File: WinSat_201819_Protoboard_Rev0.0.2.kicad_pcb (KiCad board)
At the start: 4 copper layers, 64 parts, among them J1 Conn_01x02_Female, J2 Conn_01x02_Female, J3 Conn_01x02_Female, J4 Conn_01x02_Female, J5 Conn_01x03_Female, J6 Conn_01x02_Female, P1 TPS82150, U1 SSM3K329R, U10 XBEE_PRO900, U2 SSM3K329R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

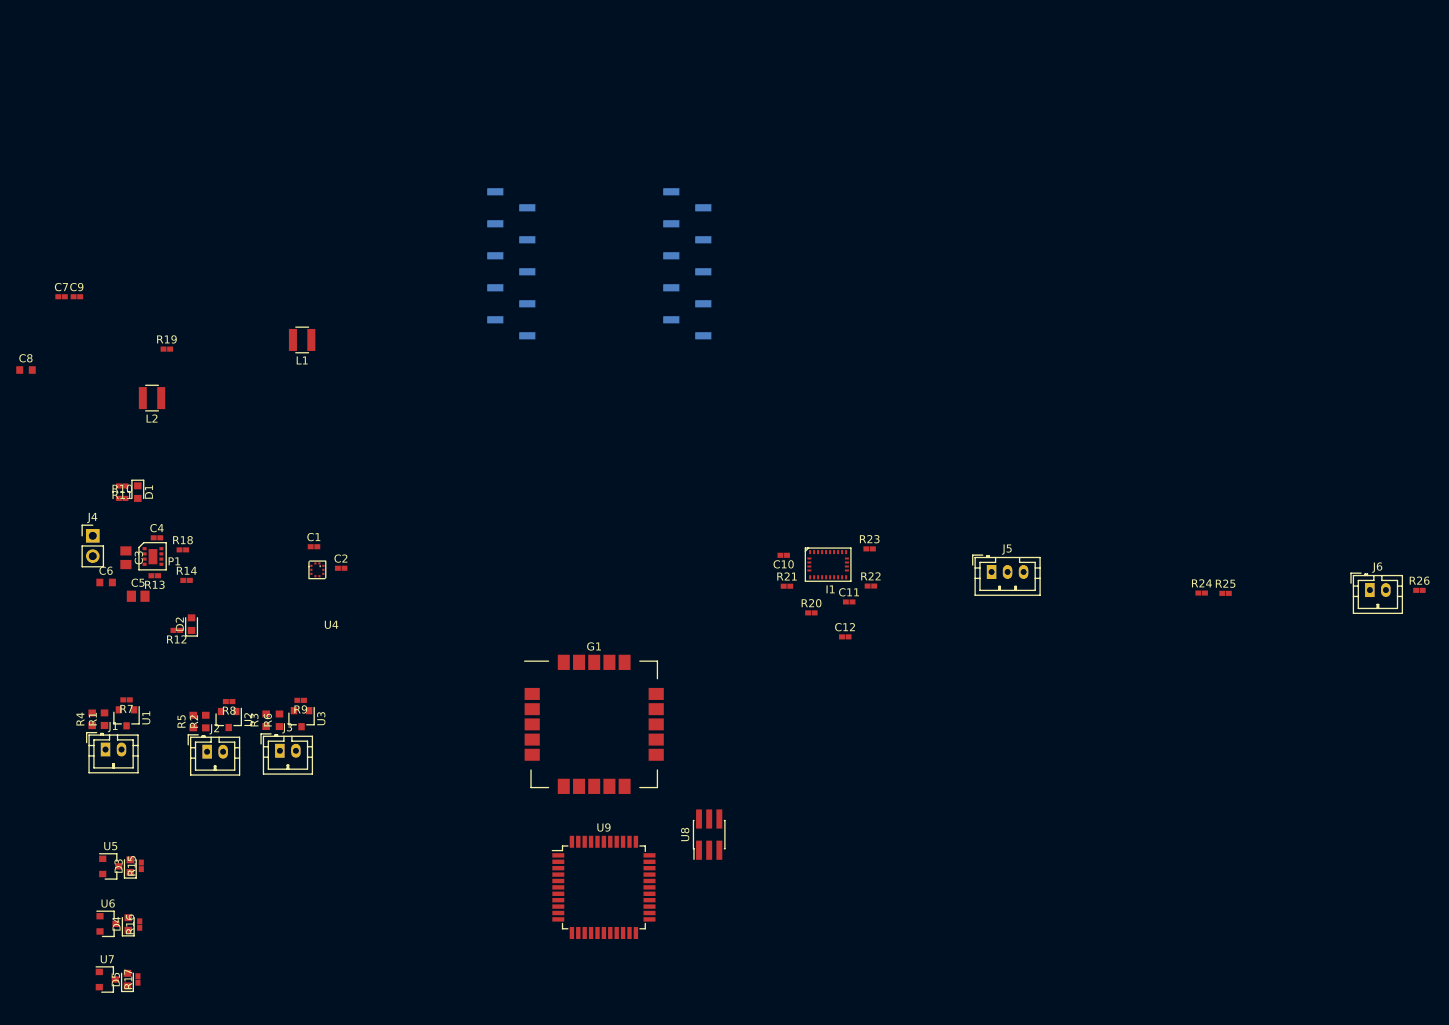
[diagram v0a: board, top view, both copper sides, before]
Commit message: net to power and pcb updates
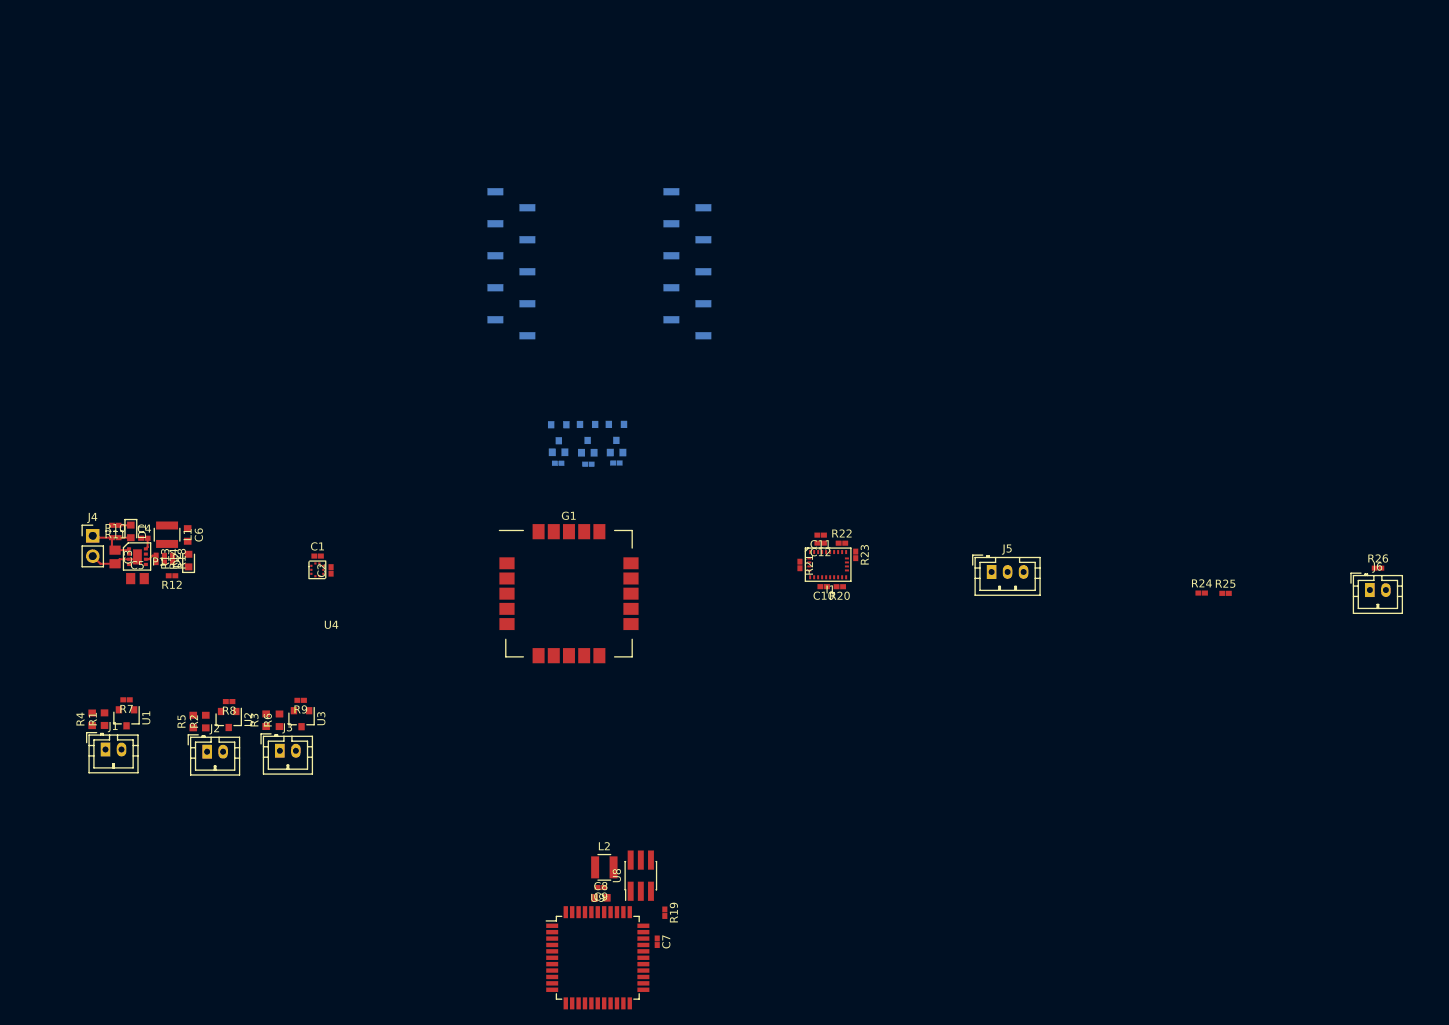
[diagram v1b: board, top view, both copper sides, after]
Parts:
- D3, D4, D5, R15, R16, R17, U5, U6, U7: moved to B.Cu
- moved C7 109.7 mm to (88.9, 181.7), turned to 270 degrees
- moved C9 98.7 mm to (81.9, 174.9), turned to 180 degrees
- moved C8 97.6 mm to (81.9, 176.2)
- moved R19 94.0 mm to (89.9, 178.0), turned to 270 degrees
- moved U7 93.4 mm to (83.8, 118.0), turned to 270 degrees
- moved D5 89.9 mm to (83.8, 120.5), turned to 180 degrees
- moved R17 88.0 mm to (83.8, 121.8), turned to 180 degrees
- moved U6 85.8 mm to (80.2, 118.0), turned to 270 degrees
- moved D4 82.3 mm to (80.2, 120.5), turned to 180 degrees
- moved L2 81.5 mm to (82.3, 172.4), turned to 180 degrees
- moved R16 80.4 mm to (80.3, 122.0), turned to 180 degrees
- moved U5 77.9 mm to (76.6, 118.0), turned to 270 degrees
- moved D3 74.4 mm to (76.6, 120.5), turned to 180 degrees
- moved R15 72.4 mm to (76.5, 121.9), turned to 180 degrees
- moved L1 29.6 mm to (27.6, 130.8), turned to 90 degrees
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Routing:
- net BAT_POS: track 0.00 -> 6.68 mm
- net GND: track 0.00 -> 6.58 mm
- net Net-(D1-Pad1): track 0.00 -> 1.55 mm
- net Net-(D1-Pad2): track 0.00 -> 1.54 mm
- net Net-(P1-Pad6): track 0.00 -> 1.47 mm
- net Net-(C4-Pad2): track 0.00 -> 1.42 mm

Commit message: Near Complete Prototype
Still needed:
Camera Control
Servo Control
Ground Plane
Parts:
- removed D3, D4, D5: LED, LED_SMD:LED_0603_1608Metric
- removed R15, R16, R17: 400 OHM, Resistor_SMD:R_0402_1005Metric
- removed U1, U2, U3, U5, U6, U7: SSM3K329R, Package_TO_SOT_SMD:SOT-23
- removed U8: JTAG-6PIN, Connector_PinHeader_1.27mm:PinHeader_2x03_P1.27mm_Vertical_SMD
- added J7: JTAG-6PIN, Connector_PinHeader_1.27mm:PinHeader_2x03_P1.27mm_Vertical_SMD, B.Cu at (77.0, 81.4)
- added Q1: SSM3K329R, Package_TO_SOT_SMD:SOT-23, F.Cu at (92.0, 116.8)
- added Q2: SSM3K329R, Package_TO_SOT_SMD:SOT-23, F.Cu at (84.8, 116.8)
- added Q3: SSM3K329R, Package_TO_SOT_SMD:SOT-23, F.Cu at (77.6, 116.8)
- C7, C8, C9, L2, R19, R24, R25, U9: moved to B.Cu
- moved R26 102.0 mm to (94.1, 78.5)
- moved J6 99.0 mm to (95.0, 83.8), turned to 90 degrees
- moved C7 92.3 mm to (74.9, 90.4)
- moved R19 92.2 mm to (75.7, 86.9)
- moved R25 92.2 mm to (84.5, 85.1)
- moved U9 91.3 mm to (82.3, 92.4), turned to 180 degrees
- moved L2 91.3 mm to (81.5, 81.1), turned to 0 degrees
- moved C9 91.3 mm to (82.0, 83.6), turned to 0 degrees
- moved C8 91.3 mm to (81.9, 84.9), turned to 180 degrees
- moved R24 88.1 mm to (86.6, 85.1)
- moved J1 87.0 mm to (94.6, 112.9), turned to 180 degrees
- moved R4 86.4 mm to (96.2, 116.7), turned to 270 degrees
- moved R1 83.6 mm to (94.7, 116.7), turned to 270 degrees
- moved R7 76.5 mm to (91.9, 119.1), turned to 0 degrees
- moved J2 70.8 mm to (87.4, 112.9), turned to 180 degrees
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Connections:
- net 3.3V renamed +3V3
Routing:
- net GND: track 6.58 -> 88.1 mm, vias 0 -> 23
- net +3V3: track 0.00 -> 58.6 mm, vias 0 -> 17
- net BAT_POS: track 6.68 -> 51.3 mm
- net MOSFET1_GPIO: track 0.00 -> 28.5 mm, vias 0 -> 1
- net MOSFET2_GPIO: track 0.00 -> 26.0 mm, vias 0 -> 1
- net IMU_SDA: track 0.00 -> 25.6 mm, vias 0 -> 2
- net MOSFET0_GPIO: track 0.00 -> 23.8 mm, vias 0 -> 1
- net GPS_TX-MCU_RX: track 0.00 -> 23.4 mm, vias 0 -> 1
- net GPS_RX-MCU_TX: track 0.00 -> 22.5 mm, vias 0 -> 1
- net IMU_SCL: track 0.00 -> 22.5 mm, vias 0 -> 2
- net XBEE_TX-MCU_RX: track 0.00 -> 14.6 mm
- net Net-(C5-Pad1): track 0.00 -> 13.6 mm
- net TEMP_SENSE-ADC: track 0.00 -> 13.3 mm
- net Net-(J7-Pad5): track 0.00 -> 7.72 mm
- net TACH_ADC: track 0.00 -> 7.16 mm
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- added copper zone on In1.Cu, net +3V3
- added copper zone on F.Cu, net BAT_POS
- added copper zone on In2.Cu, net GND
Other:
- board outline added: 36 x 62 mm
- net class Default: clearance 0.2 -> 0.0508; trace_width 0.25 -> 0.1
- rule trace_clearance: 0.2 -> 0.0508
- rule trace_min: 0.2 -> 0.006

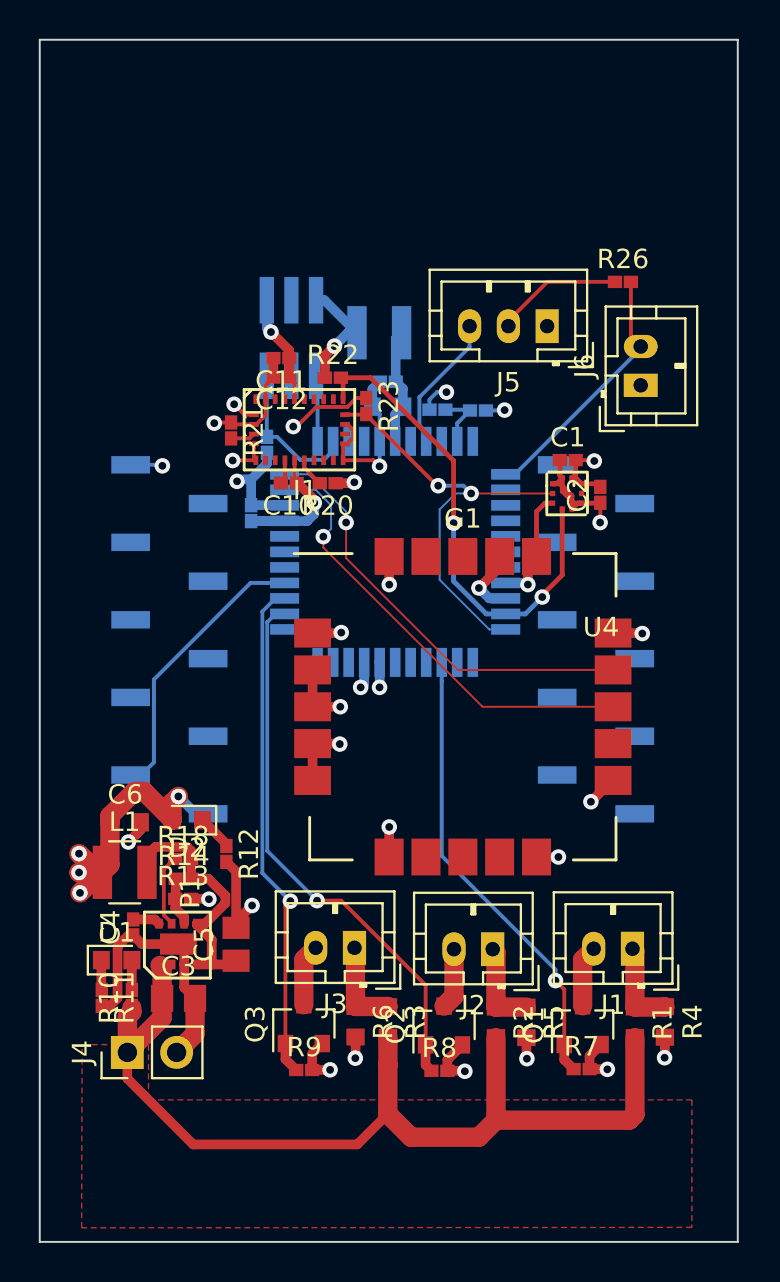
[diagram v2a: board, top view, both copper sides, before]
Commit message: V1.0.0
First Complete Revision

To Do:
-Double check schematic and PCB
-Increase width of some data lines
-Add ESD Protection
--Resistor and Diodes
--ESD Dissipation 1MOhm
-Trade study M2 vs M3* (*current)
-Check application notes for BNO055 to ensure that we are in spec (stresses, RF, and such.
-Misc.
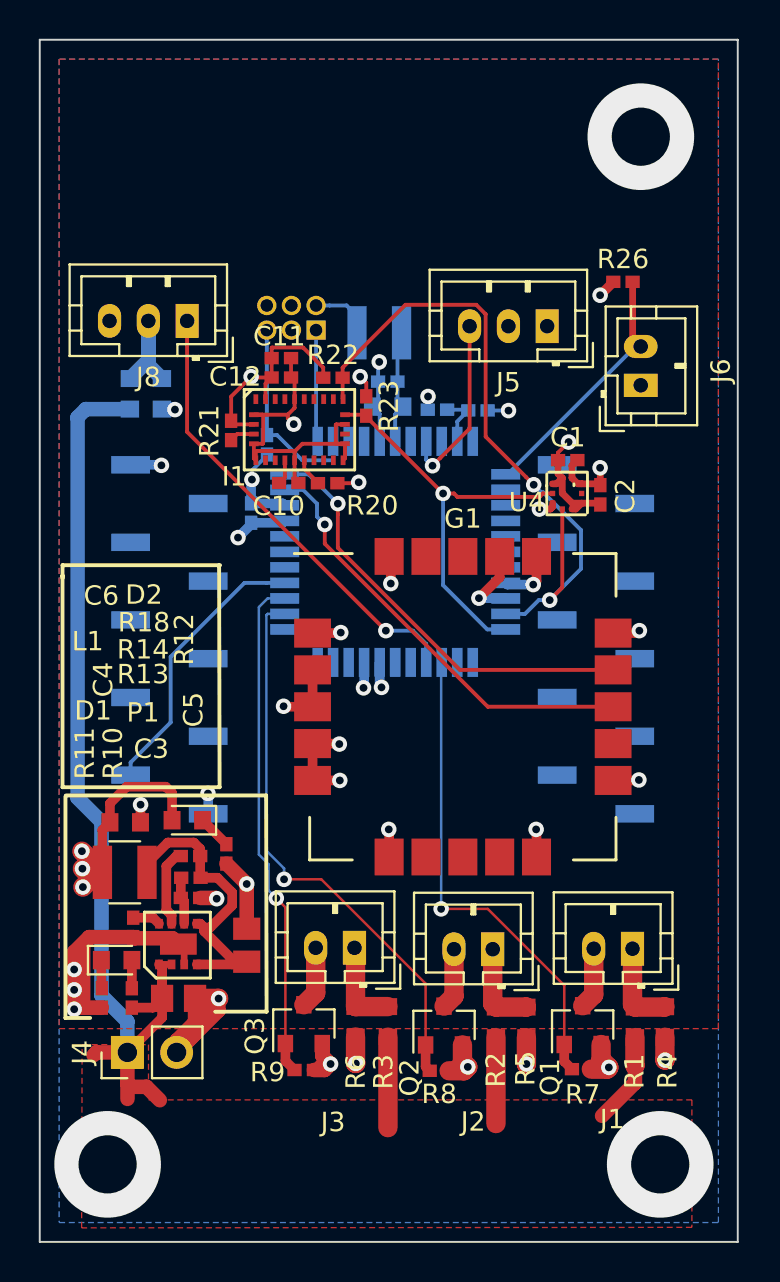
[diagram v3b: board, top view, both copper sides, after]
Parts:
- added J8: Conn_01x03_Female, Connector_JST:JST_PH_B3B-PH-K_1x03_P2.00mm_Vertical, F.Cu at (71.6, 80.5)
- added R15: R_Small, Resistor_SMD:R_0603_1608Metric, B.Cu at (68.7, 84.3)
- added R16: R_Small, Resistor_SMD:R_0603_1608Metric, B.Cu at (70.3, 84.3)
- C1, C10, C11, C12, C2, C4, C7, C9: footprint Capacitor_SMD:C_0402_1005Metric -> OSD335x-KiCad-master:Not_Broken_0402
- J7: footprint Connector_PinHeader_1.27mm:PinHeader_2x03_P1.27mm_Vertical_SMD -> Connector_PinHeader_1.27mm:PinHeader_2x03_P1.27mm_Horizontal
- R10, R11, R12, R13, R14, R18, R19, R20, R21, R22, R23, R24, R25, R26, R7, R8, R9: footprint Resistor_SMD:R_0402_1005Metric -> OSD335x-KiCad-master:Not_Broken_0402
- moved J7 1.33 mm to (78.2, 81.0)
- moved C5 0.55 mm to (74.7, 112.7)
- moved R18 0.40 mm to (71.8, 108.1)
- moved R13 0.38 mm to (71.8, 110.3)
- moved R14 0.38 mm to (71.8, 109.2)
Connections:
- U9 pad 15: Net-(U9-Pad15) -> SERVO_TCL
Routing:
- net SERVO_TCL: track 0.00 -> 23.5 mm, vias 0 -> 1
- net BAT_POS: track 51.3 -> 65.8 mm
- net IMU_SDA: track 25.6 -> 35.6 mm
- net GND: track 88.1 -> 97.9 mm, vias 23 -> 31
- net Net-(J8-Pad2): track 0.00 -> 6.63 mm
- net Net-(J7-Pad5): track 7.72 -> 10.3 mm
- net +3V3: track 58.6 -> 56.2 mm
- net Net-(J7-Pad1): track 3.41 -> 5.77 mm
- net TACH_ADC: track 7.16 -> 9.39 mm, vias 0 -> 1
- net MOSFET0_GPIO: track 23.8 -> 25.2 mm
- net Net-(C5-Pad1): track 13.6 -> 14.8 mm
- net IMU_SCL: track 22.5 -> 21.5 mm, vias 2 -> 1
- net GPS_TX-MCU_RX: track 23.4 -> 22.5 mm
- net MOSFET1_GPIO: track 28.5 -> 29.1 mm
- added copper zone on B.Cu, net GND
- added copper zone on F.Cu, net GND
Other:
- net class Default: clearance 0.0508 -> 0.127; trace_width 0.1 -> 0.2
- rule trace_clearance: 0.0508 -> 0.127
- rule trace_min: 0.006 -> 0.127
- rule via_min_drill: 0.3 -> 0.254
- rule via_min_size: 0.4 -> 0.4572

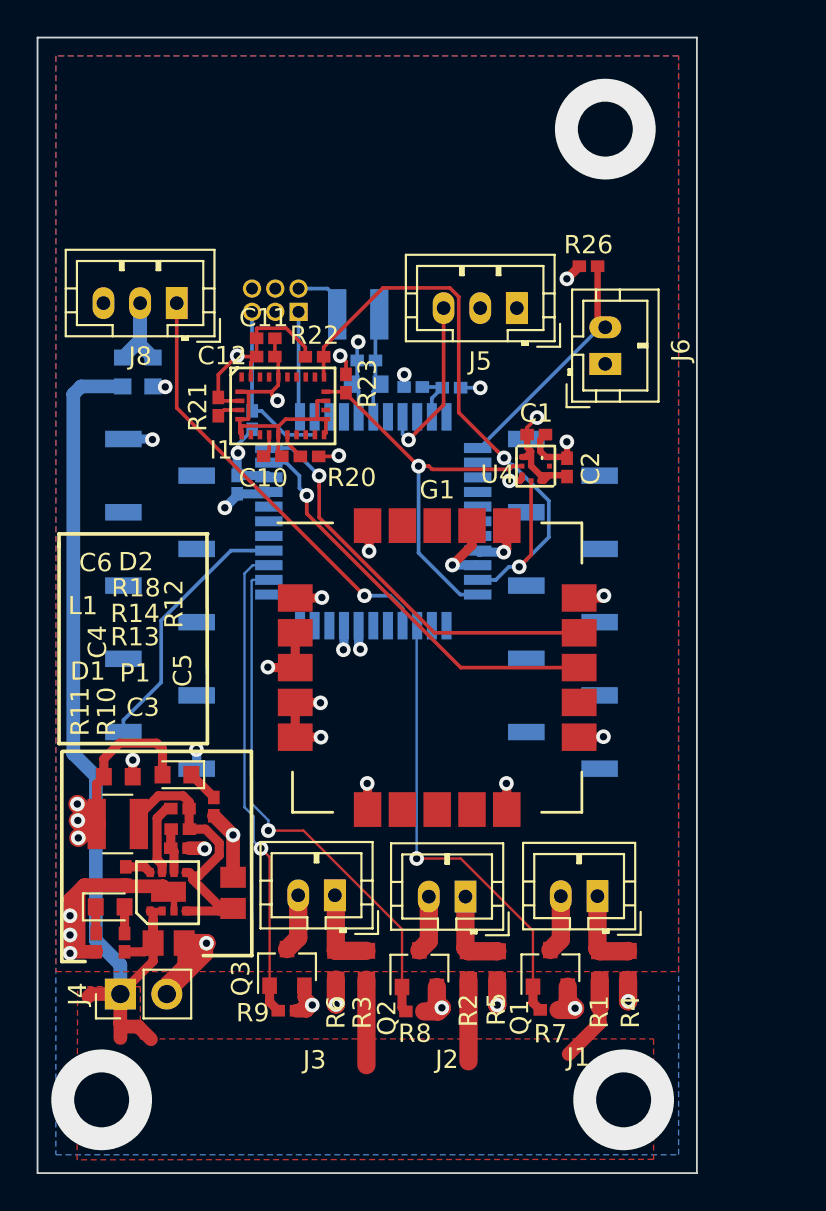
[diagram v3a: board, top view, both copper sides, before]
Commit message: V1.1.0  GPS Module Change
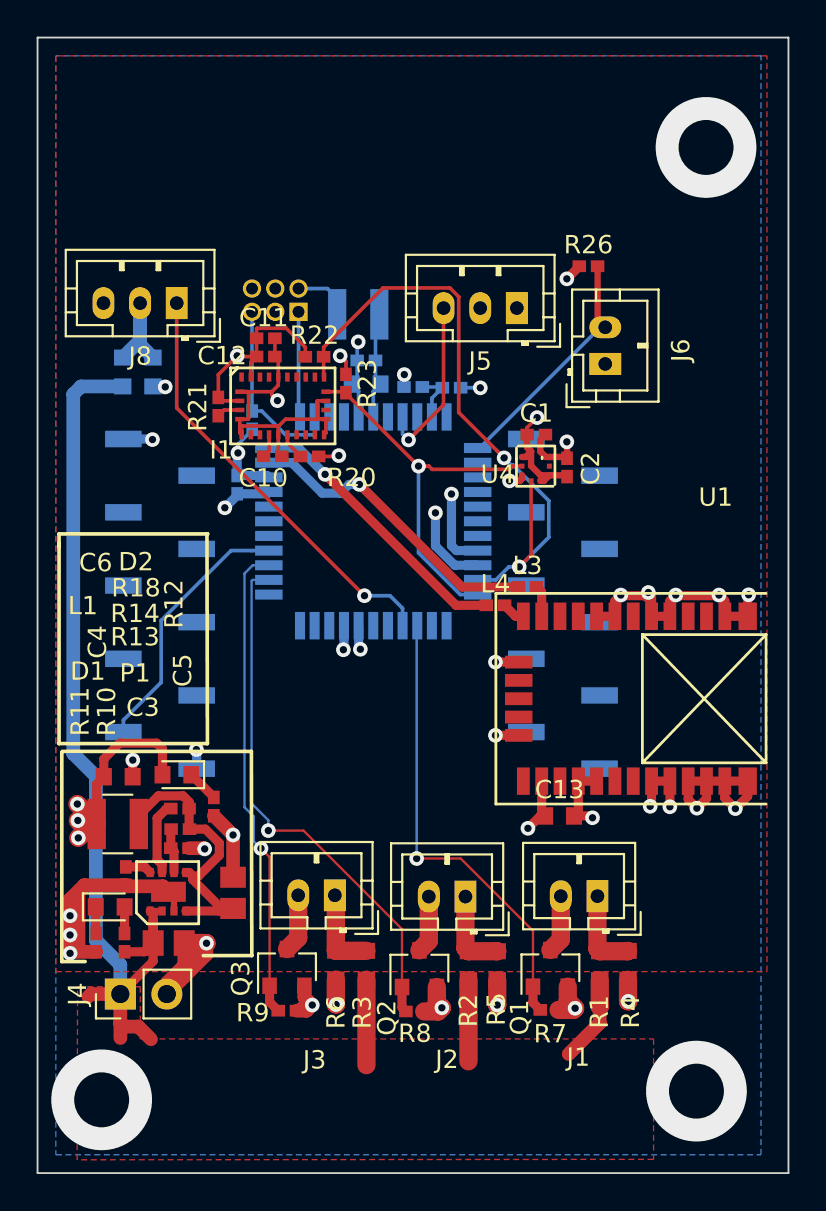
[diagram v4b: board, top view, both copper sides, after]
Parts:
- removed G1: SAM-M8Q, OSD335x-KiCad-master:SAM-M8Q
- added C13: 4.7uF, Capacitor_SMD:C_0603_1608Metric, F.Cu at (92.5, 108.5)
- added L3: L_Small, OSD335x-KiCad-master:Not_Broken_0402, F.Cu at (90.8, 96.0)
- added L4: BLM15HD102SN1, OSD335x-KiCad-master:Not_Broken_0402, F.Cu at (89.0, 97.0)
- added U1: CAM-M8, OSD335x-KiCad-master:CAM-M8, F.Cu at (101.5, 105.6)
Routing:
- net GND: track 97.9 -> 117.5 mm, vias 31 -> 33
- net GPS_RX-MCU_TX: track 22.5 -> 15.4 mm
- net GPS_TX-MCU_RX: track 22.5 -> 16.8 mm
- net +3V3: track 56.2 -> 60.4 mm, vias 17 -> 19
- net Net-(L3-Pad2): track 0.00 -> 1.71 mm
- net Net-(L4-Pad2): track 0.00 -> 1.27 mm
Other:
- board size 36 x 62 mm -> 41 x 62 mm
